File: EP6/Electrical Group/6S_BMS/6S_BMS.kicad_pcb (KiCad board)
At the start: 2 copper layers, 100 x 70 mm, 183 parts, among them IC1 DZDH0401DW-7, J1 Cell Pads, J2 Power Out, J3 Front Panel, J4 Charge, J8 USB_C_stm32, J9 STDC14, Q1 HSBA3119, Q10 SI2301CDS-T1-GE3, Q11 SI2301CDS-T1-GE3, Q12 SI2301CDS-T1-GE3, Q13 2N7002, Q14 AO3401A, Q2 2N7002, Q3 2N7002, Q4 HSBA3119, Q6 HSBA3119, Q7 SI2301CDS-T1-GE3, Q8 SI2301CDS-T1-GE3, Q9 SI2301CDS-T1-GE3, SW1 RESET, U1 BQ7693003, U2 TCAN1042VDRQ1, U3 STM32F103C8Tx, U4 CAT24C256, U5 LM66100DCK, U6 SN74LVC8T245, U7 L78L05_SOT89, U8 XC6206PxxxMR, Y1 8MHz X49SM8MSD2SC

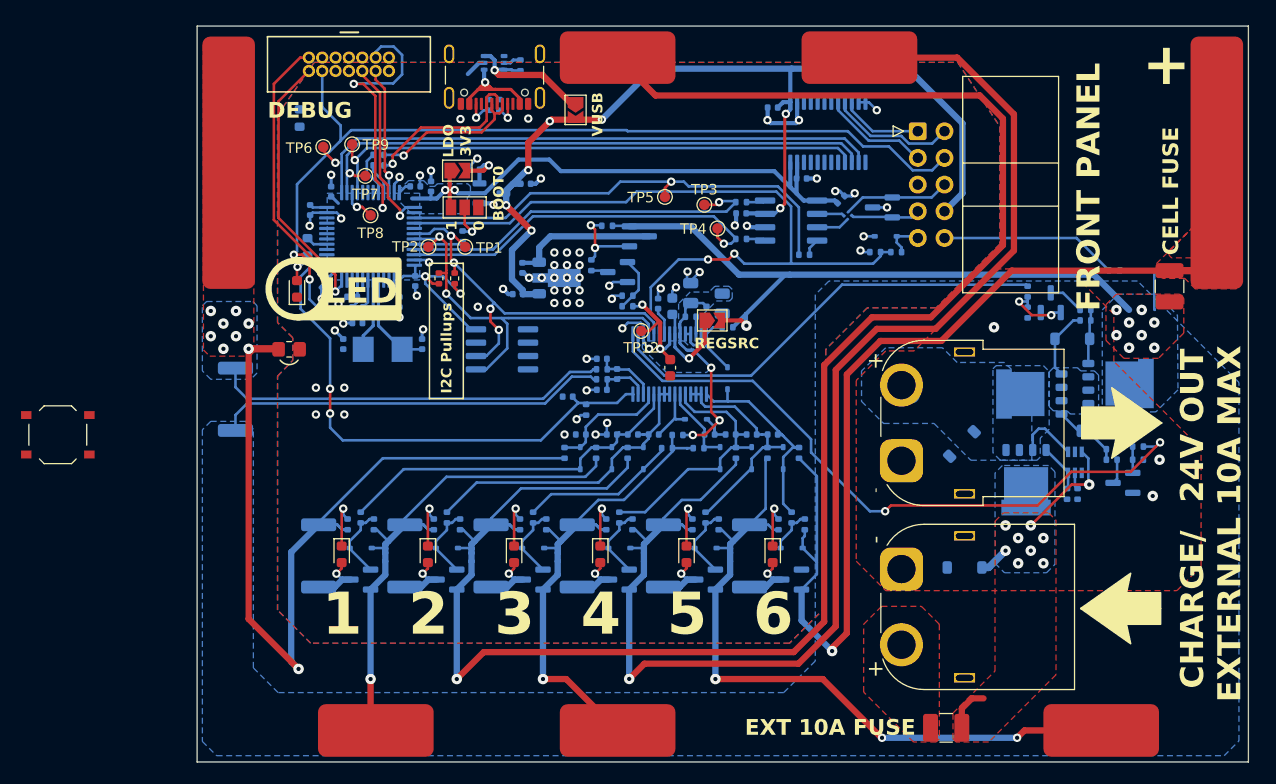
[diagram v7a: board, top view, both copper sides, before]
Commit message: added reset buttons, fix errors
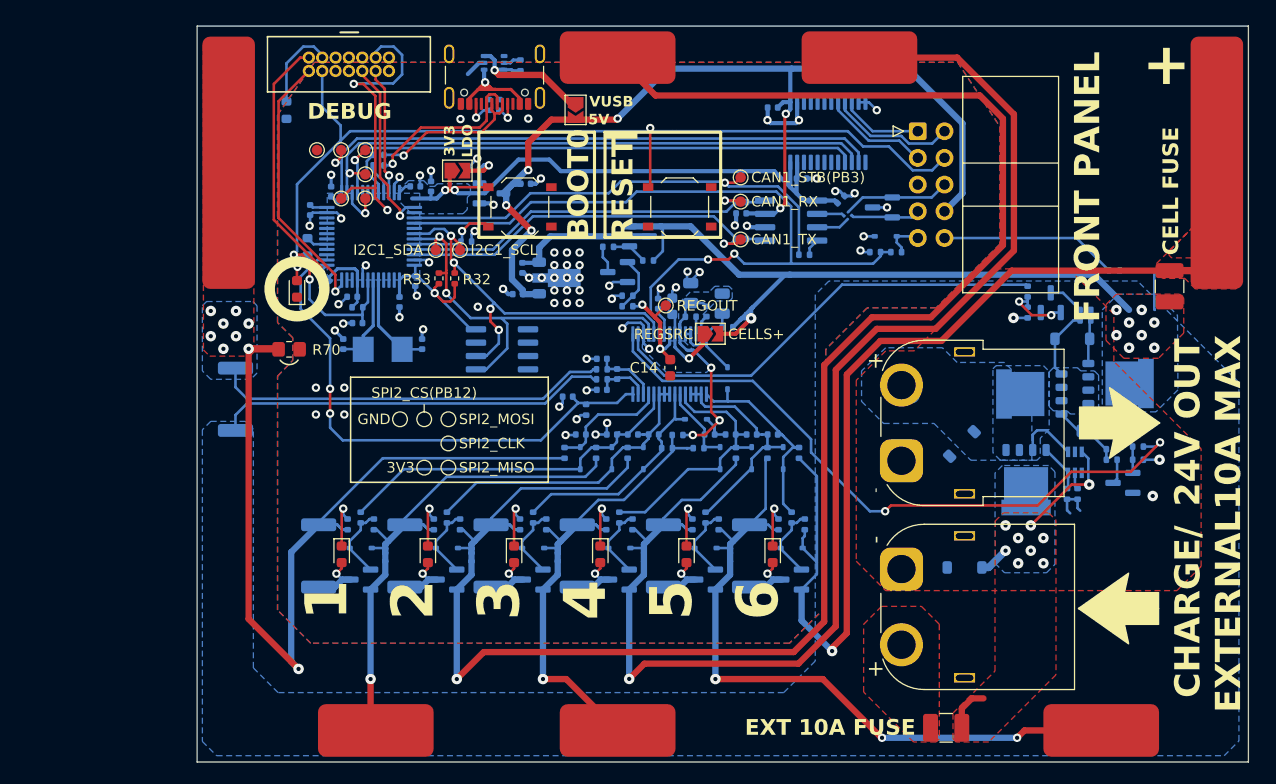
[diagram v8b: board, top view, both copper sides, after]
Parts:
- removed JP2: BOOT0, Jumper:SolderJumper-3_P1.3mm_Open_Pad1.0x1.5mm
- added SW2: BOOT0, Button_Switch_SMD:SW_Push_1P1T_XKB_TS-1187A, F.Cu at (129.2, 42.2)
- added TP10: 3V3, TestPoint:TestPoint_Pad_D1.0mm, F.Cu at (112.2, 41.4)
- added TP11: GND, TestPoint:TestPoint_Pad_D1.0mm, F.Cu at (109.9, 36.8)
- R28: value 1k -> 10k
- moved SW1 63.0 mm to (144.4, 42.2), turned to 180 degrees
- moved TP5 7.43 mm to (150.2, 39.4)
- moved R68 5.11 mm to (141.4, 47.3)
- moved TP3 3.46 mm to (150.2, 41.7)
- moved TP12 3.36 mm to (143.1, 51.6)
- moved TP4 2.44 mm to (150.2, 45.3)
- moved R69 2.37 mm to (137.6, 46.0), turned to 180 degrees
- moved TP6 1.73 mm to (112.2, 36.8)
- moved TP8 1.68 mm to (114.5, 41.4)
- moved R71 1.46 mm to (107.0, 33.0)
- moved TP9 1.37 mm to (114.5, 36.8)
- moved JP1 1.28 mm to (147.3, 54.3)
- moved TP2 0.76 mm to (121.2, 46.3)
- moved R28 0.61 mm to (124.1, 45.5), turned to 180 degrees
- moved TP1 0.58 mm to (123.5, 46.3)
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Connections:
- R28 pad 1: Net-(JP2-C) -> GND
- SW1 pad 1: /MCU_RST -> GND
- SW1 pad 2: GND -> /MCU_RST
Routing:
- net /MCU/GNDDetect: track 0.00 -> 8.27 mm
- net /PACK-: track 37.4 -> 44.0 mm
- net /MCU_RST: track 95.0 -> 100.9 mm, vias 2 -> 3
- net /CELLS+: track 67.6 -> 72.5 mm
- net Net-(Q14-G): track 8.08 -> 3.41 mm, vias 2 -> 0
- net /MCU/BOOT0: track 4.69 -> 8.50 mm, vias 0 -> 1
- net Net-(JP2-C): track 3.51 -> 0.00 mm, vias 1 -> 0
- net +3V3: track 108.4 -> 111.6 mm, vias 6 -> 5
- net GND: track 62.9 -> 66.1 mm, vias 68 -> 70
- net Net-(D10-A): track 4.29 -> 7.16 mm
- net /MCU/OSC_OUT: track 6.98 -> 8.89 mm
- net /C3: track 20.4 -> 21.8 mm
- net /AFE/REGSRC: track 9.22 -> 7.88 mm
- net Net-(Q13-D): track 1.62 -> 2.60 mm
- net /MCU/SPI2_MISO: track 3.27 -> 4.09 mm
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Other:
- board text added: "5V"
- board text added: "CAN1_RX"
- board text added: "CAN1_STB(PB3)"
- board text added: "CAN1_TX"
- board text added: "CELLS+"
- board text added: "GND"
- board text added: "I2C1_SCL"
- board text added: "I2C1_SDA"
- board text added: "REGOUT"
- board text added: "RESET"
- board text added: "SPI2_CLK"
- board text added: "SPI2_CS(PB12)"
- board text added: "SPI2_MISO"
- board text added: "SPI2_MOSI"
- board text removed: "0"
- board text removed: "I2C Pullups"
- board text removed: "LED"
